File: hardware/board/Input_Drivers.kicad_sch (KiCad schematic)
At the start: 14 parts

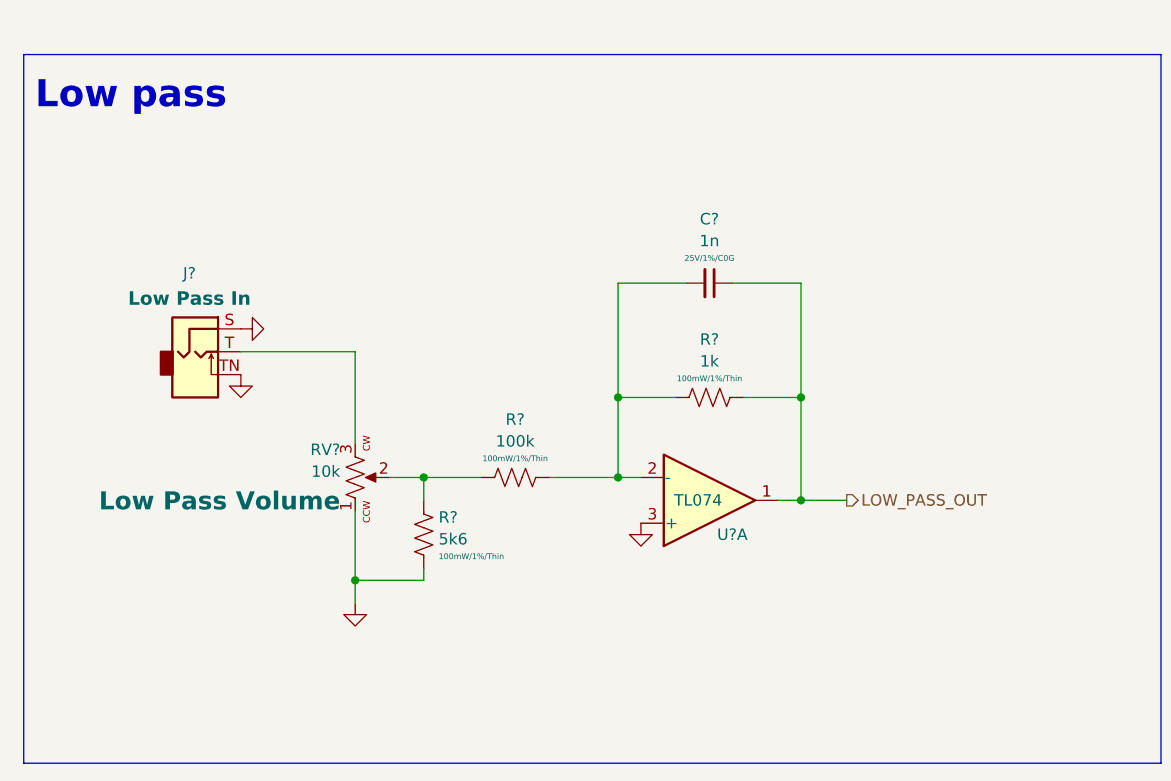
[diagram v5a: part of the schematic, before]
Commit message: Schematic and PCB updates to add offset trim
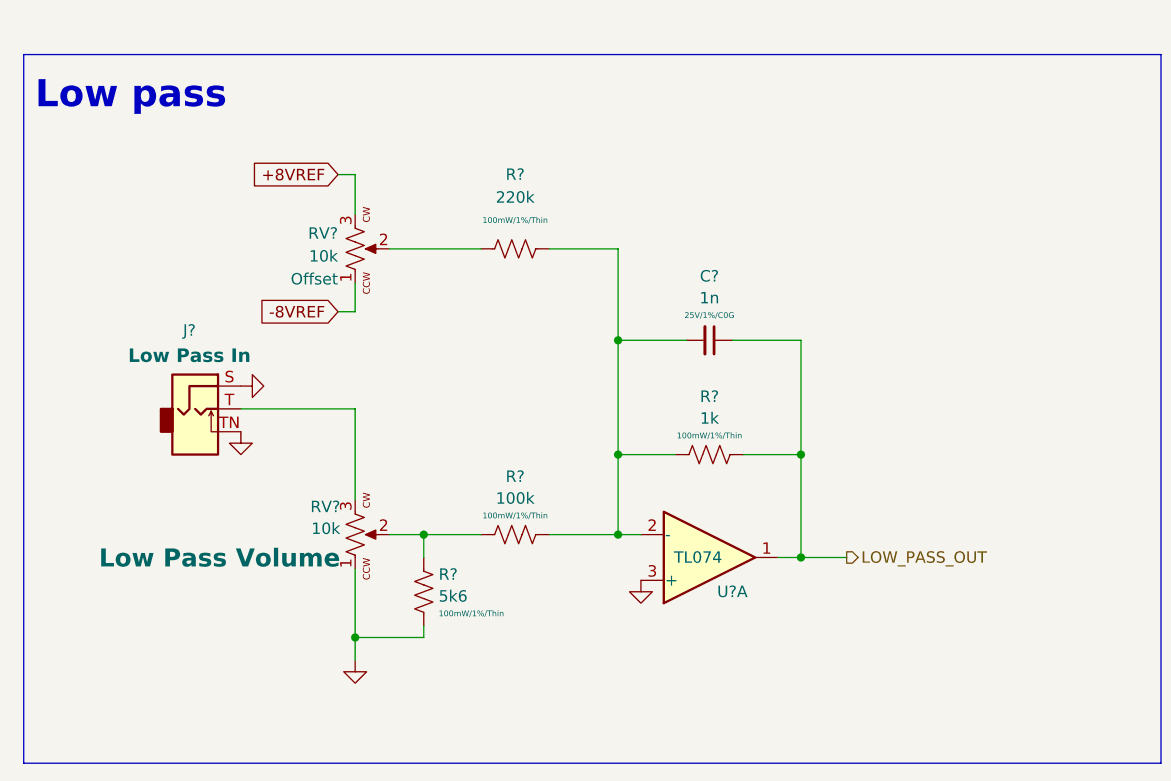
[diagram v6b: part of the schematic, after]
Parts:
- added R?: 220k, winterbloom:R_0603_HandSolder, symbol Device:R_US
- added RV?: 10k, Potentiometer_SMD:Potentiometer_Bourns_TC33X_Vertical, symbol winterbloom:Eurorack_Pot
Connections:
- net at C?.2, R?.1, R?.2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: now also R?.1
- new net: R?.2, RV?.2
- new net +8VREF: RV?.3
- new net -8VREF: RV?.1
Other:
- moved on the sheet: C?, J?, R?, RV?, U?A

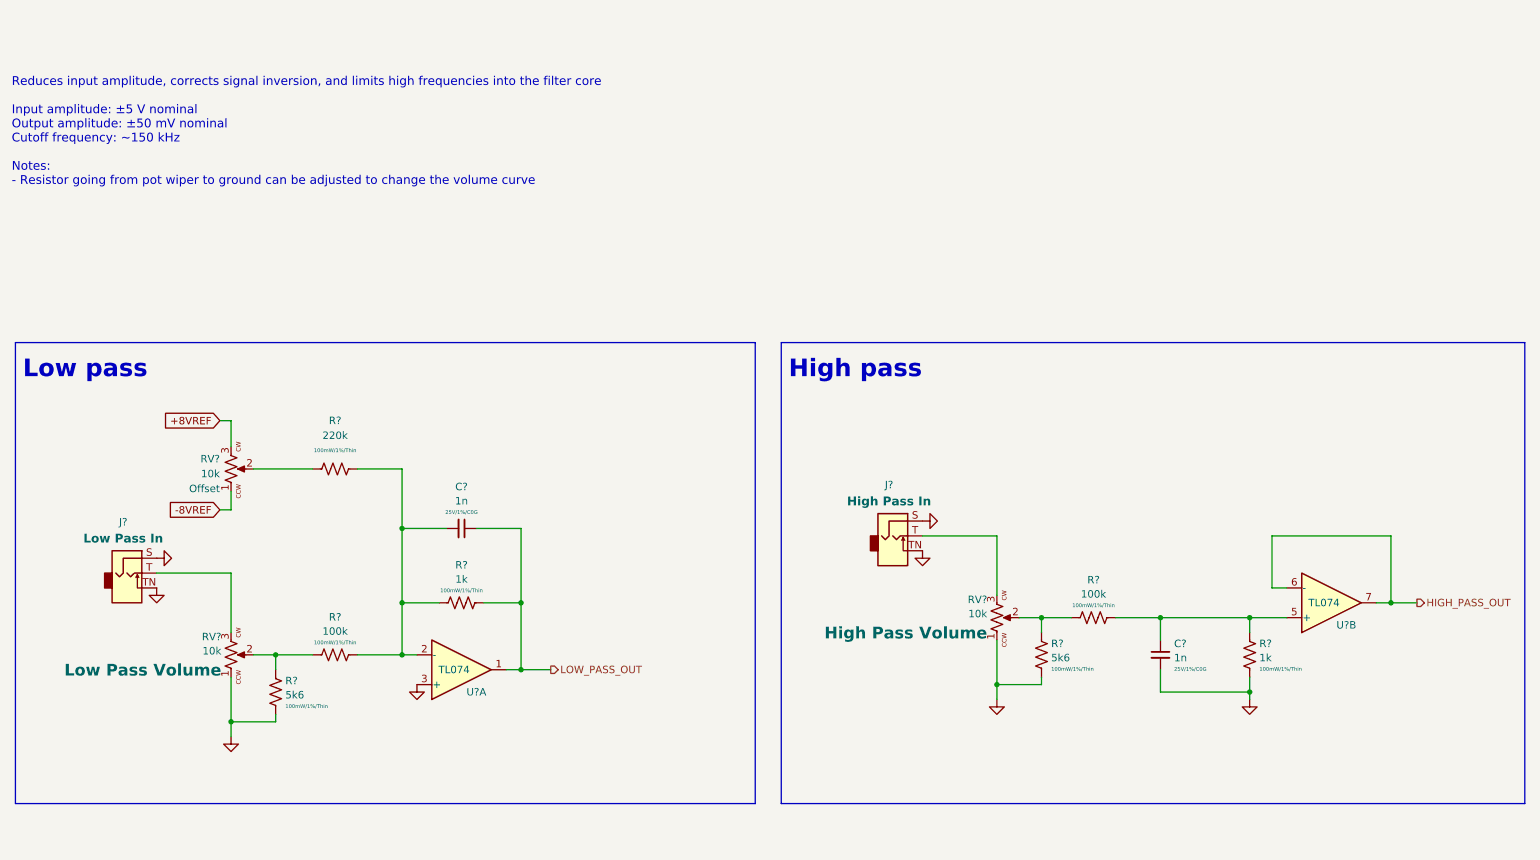
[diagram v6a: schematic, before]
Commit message: hardware: finalize v3
- Updated version number and release date
- Swapped TL074C to TL074H
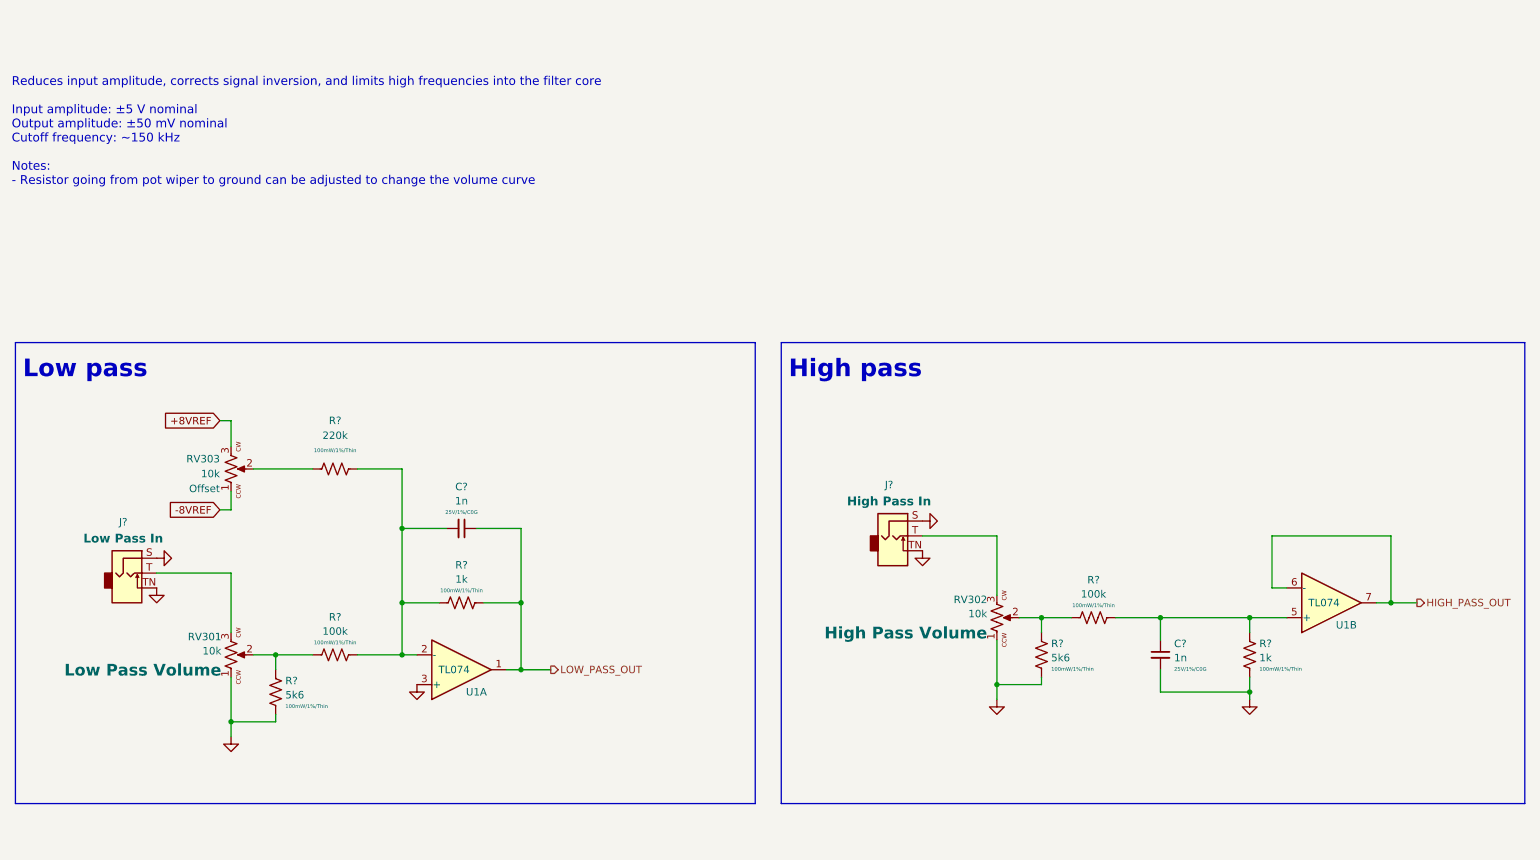
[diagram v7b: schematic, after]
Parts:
- U1: renamed from U?; DigiKey 296-7198-1-ND -> 296-TL074HIPWRCT-ND; LCSC C96507 -> C4370424; MPN TL074CPWR -> TL074HIPWR; Notes (none) -> TL074H over TL074C due to better input offset voltage
- gave numbers to parts that had none: 3
